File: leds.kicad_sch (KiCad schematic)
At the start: 64 parts

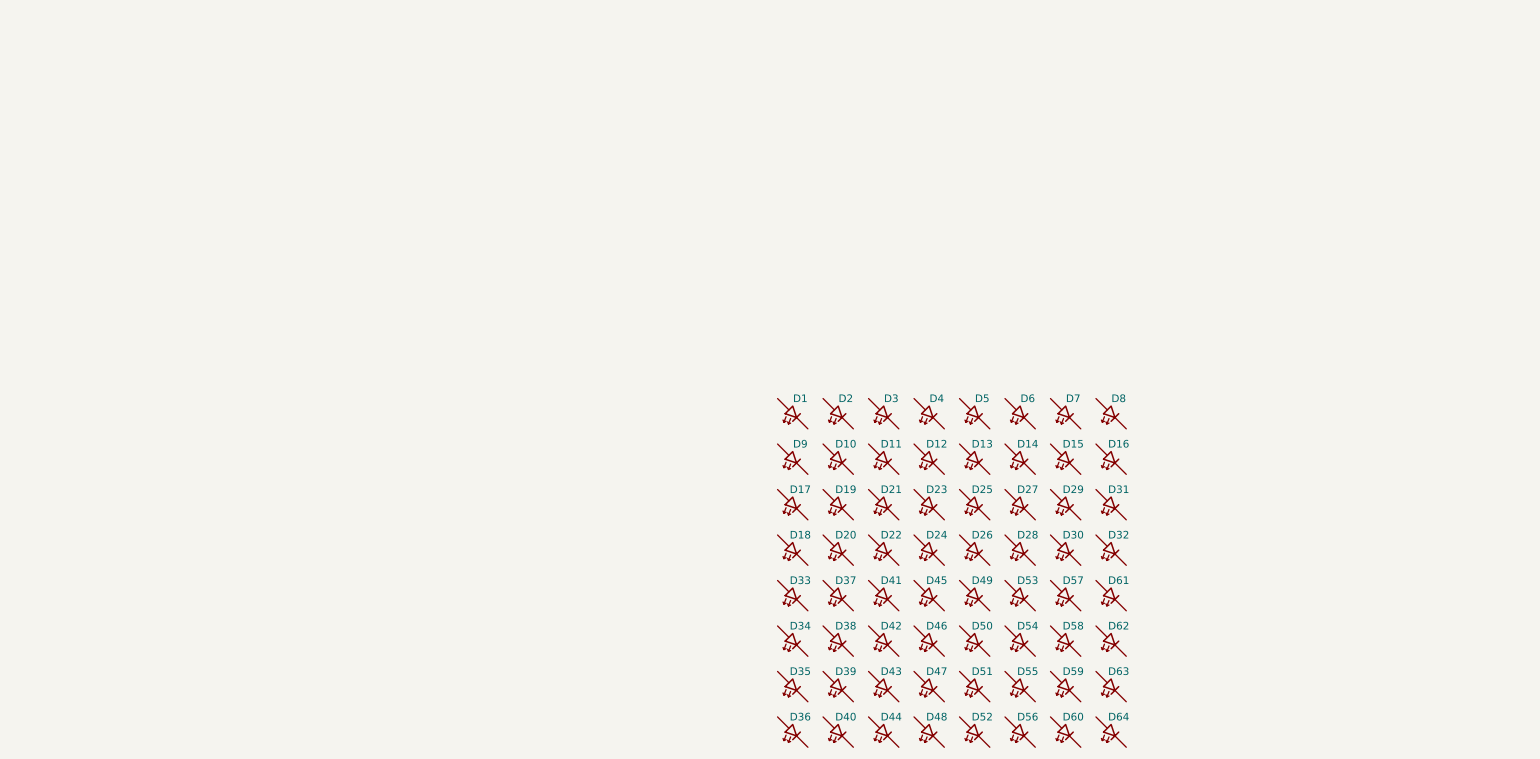
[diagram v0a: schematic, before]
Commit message: Added the led driver chip and connected all the pins
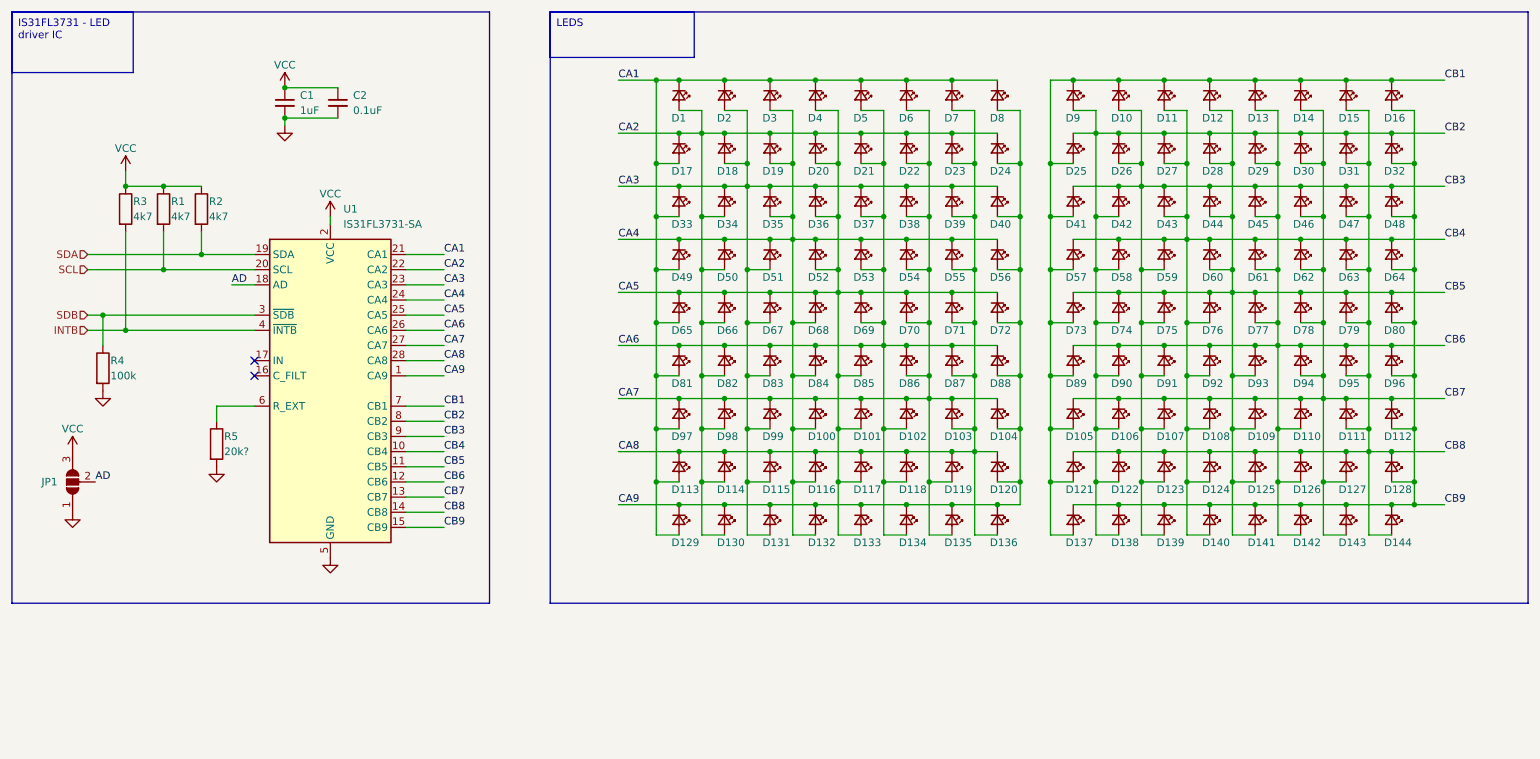
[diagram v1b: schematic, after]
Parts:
- removed D1, D10, D11, D12, D13, D14, D15, D16, D17, D18, D19, D2, D20, D21, D22, D23, D24, D25, D26, D27, D28, D29, D3, D30, D31, D32, D33, D34, D35, D36, D37, D38, D39, D4, D40, D41, D42, D43, D44, D45, D46, D47, D48, D49, D5, D50, D51, D52, D53, D54, D55, D56, D57, D58, D59, D6, D60, D61, D62, D63, D64, D7, D8, D9: LED_45deg, symbol Device:LED_45deg
- added C1: 1uF, symbol Device:C_Small
- added C2: 0.1uF, symbol Device:C_Small
- added D1, D10, D100, D101, D102, D103, D104, D105, D106, D107, D108, D109, D11, D110, D111, D112, D113, D114, D115, D116, D117, D118, D119, D12, D120, D121, D122, D123, D124, D125, D126, D127, D128, D129, D13, D130, D131, D132, D133, D134, D135, D136, D137, D138, D139, D14, D140, D141, D142, D143, D144, D15, D16, D17, D18, D19, D2, D20, D21, D22, D23, D24, D25, D26, D27, D28, D29, D3, D30, D31, D32, D33, D34, D35, D36, D37, D38, D39, D4, D40, D41, D42, D43, D44, D45, D46, D47, D48, D49, D5, D50, D51, D52, D53, D54, D55, D56, D57, D58, D59, D6, D60, D61, D62, D63, D64, D65, D66, D67, D68, D69, D7, D70, D71, D72, D73, D74, D75, D76, D77, D78, D79, D8, D80, D81, D82, D83, D84, D85, D86, D87, D88, D89, D9, D90, D91, D92, D93, D94, D95, D96, D97, D98, D99: LED_Small, symbol Device:LED_Small
- added JP1: SolderJumper_3_Open, symbol Jumper:SolderJumper_3_Open
- added R1, R2, R3: 4k7, symbol Device:R
- added R4: 100k, symbol Device:R
- added R5: 20k?, symbol Device:R
- added U1: IS31FL3731-SA, Package_SO:SSOP-28_5.3x10.2mm_P0.65mm, symbol Driver_LED:IS31FL3731-SA
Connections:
- new net: R5.1, U1.6 (R_EXT)
- new net AD: JP1.2 (C), U1.18 (AD)
- new net CA1: D1.1 (K), D113.2 (A), D129.2 (A), D17.2 (A), D2.1 (K), D3.1 (K), D33.2 (A), D4.1 (K), D49.2 (A), D5.1 (K), D6.1 (K), D65.2 (A), D7.1 (K), D8.1 (K), D81.2 (A), D97.2 (A), U1.21 (CA1)
- new net CA2: D1.2 (A), D114.2 (A), D130.2 (A), D17.1 (K), D18.1 (K), D19.1 (K), D20.1 (K), D21.1 (K), D22.1 (K), D23.1 (K), D24.1 (K), D34.2 (A), D50.2 (A), D66.2 (A), D82.2 (A), D98.2 (A), U1.22 (CA2)
- new net CA3: D115.2 (A), D131.2 (A), D18.2 (A), D2.2 (A), D33.1 (K), D34.1 (K), D35.1 (K), D36.1 (K), D37.1 (K), D38.1 (K), D39.1 (K), D40.1 (K), D51.2 (A), D67.2 (A), D83.2 (A), D99.2 (A), U1.23 (CA3)
- new net CA4: D100.2 (A), D116.2 (A), D132.2 (A), D19.2 (A), D3.2 (A), D35.2 (A), D49.1 (K), D50.1 (K), D51.1 (K), D52.1 (K), D53.1 (K), D54.1 (K), D55.1 (K), D56.1 (K), D68.2 (A), D84.2 (A), U1.24 (CA4)
- new net CA5: D101.2 (A), D117.2 (A), D133.2 (A), D20.2 (A), D36.2 (A), D4.2 (A), D52.2 (A), D65.1 (K), D66.1 (K), D67.1 (K), D68.1 (K), D69.1 (K), D70.1 (K), D71.1 (K), D72.1 (K), D85.2 (A), U1.25 (CA5)
- new net CA6: D102.2 (A), D118.2 (A), D134.2 (A), D21.2 (A), D37.2 (A), D5.2 (A), D53.2 (A), D69.2 (A), D81.1 (K), D82.1 (K), D83.1 (K), D84.1 (K), D85.1 (K), D86.1 (K), D87.1 (K), D88.1 (K), U1.26 (CA6)
- new net CA7: D100.1 (K), D101.1 (K), D102.1 (K), D103.1 (K), D104.1 (K), D119.2 (A), D135.2 (A), D22.2 (A), D38.2 (A), D54.2 (A), D6.2 (A), D70.2 (A), D86.2 (A), D97.1 (K), D98.1 (K), D99.1 (K), U1.27 (CA7)
- new net CA8: D103.2 (A), D113.1 (K), D114.1 (K), D115.1 (K), D116.1 (K), D117.1 (K), D118.1 (K), D119.1 (K), D120.1 (K), D136.2 (A), D23.2 (A), D39.2 (A), D55.2 (A), D7.2 (A), D71.2 (A), D87.2 (A), U1.28 (CA8)
- new net CA9: D104.2 (A), D120.2 (A), D129.1 (K), D130.1 (K), D131.1 (K), D132.1 (K), D133.1 (K), D134.1 (K), D135.1 (K), D136.1 (K), D24.2 (A), D40.2 (A), D56.2 (A), D72.2 (A), D8.2 (A), D88.2 (A), U1.1 (CA9)
- new net CB1: D10.1 (K), D105.2 (A), D11.1 (K), D12.1 (K), D121.2 (A), D13.1 (K), D137.2 (A), D14.1 (K), D15.1 (K), D16.1 (K), D25.2 (A), D41.2 (A), D57.2 (A), D73.2 (A), D89.2 (A), D9.1 (K), U1.7 (CB1)
- new net CB2: D106.2 (A), D122.2 (A), D138.2 (A), D25.1 (K), D26.1 (K), D27.1 (K), D28.1 (K), D29.1 (K), D30.1 (K), D31.1 (K), D32.1 (K), D42.2 (A), D58.2 (A), D74.2 (A), D9.2 (A), D90.2 (A), U1.8 (CB2)
- new net CB3: D10.2 (A), D107.2 (A), D123.2 (A), D139.2 (A), D26.2 (A), D41.1 (K), D42.1 (K), D43.1 (K), D44.1 (K), D45.1 (K), D46.1 (K), D47.1 (K), D48.1 (K), D59.2 (A), D75.2 (A), D91.2 (A), U1.9 (CB3)
- new net CB4: D108.2 (A), D11.2 (A), D124.2 (A), D140.2 (A), D27.2 (A), D43.2 (A), D57.1 (K), D58.1 (K), D59.1 (K), D60.1 (K), D61.1 (K), D62.1 (K), D63.1 (K), D64.1 (K), D76.2 (A), D92.2 (A), U1.10 (CB4)
- new net CB5: D109.2 (A), D12.2 (A), D125.2 (A), D141.2 (A), D28.2 (A), D44.2 (A), D60.2 (A), D73.1 (K), D74.1 (K), D75.1 (K), D76.1 (K), D77.1 (K), D78.1 (K), D79.1 (K), D80.1 (K), D93.2 (A), U1.11 (CB5)
- new net CB6: D110.2 (A), D126.2 (A), D13.2 (A), D142.2 (A), D29.2 (A), D45.2 (A), D61.2 (A), D77.2 (A), D89.1 (K), D90.1 (K), D91.1 (K), D92.1 (K), D93.1 (K), D94.1 (K), D95.1 (K), D96.1 (K), U1.12 (CB6)
- new net CB7: D105.1 (K), D106.1 (K), D107.1 (K), D108.1 (K), D109.1 (K), D110.1 (K), D111.1 (K), D112.1 (K), D127.2 (A), D14.2 (A), D143.2 (A), D30.2 (A), D46.2 (A), D62.2 (A), D78.2 (A), D94.2 (A), U1.13 (CB7)
- new net CB8: D111.2 (A), D121.1 (K), D122.1 (K), D123.1 (K), D124.1 (K), D125.1 (K), D126.1 (K), D127.1 (K), D128.1 (K), D144.2 (A), D15.2 (A), D31.2 (A), D47.2 (A), D63.2 (A), D79.2 (A), D95.2 (A), U1.14 (CB8)
- new net CB9: D112.2 (A), D128.2 (A), D137.1 (K), D138.1 (K), D139.1 (K), D140.1 (K), D141.1 (K), D142.1 (K), D143.1 (K), D144.1 (K), D16.2 (A), D32.2 (A), D48.2 (A), D64.2 (A), D80.2 (A), D96.2 (A), U1.15 (CB9)
- new net GND: C1.2, C2.2, JP1.1 (A), R4.2, R5.2, U1.5 (GND)
- new net INTB: R3.2, U1.4 (~{INTB})
- new net SCL: R1.2, U1.20 (SCL)
- new net SDA: R2.2, U1.19 (SDA)
- new net SDB: R4.1, U1.3 (~{SDB})
- new net VCC: C1.1, C2.1, JP1.3 (B), R1.1, R2.1, R3.1, U1.2 (VCC)
- no-connect marks 0 -> 2
